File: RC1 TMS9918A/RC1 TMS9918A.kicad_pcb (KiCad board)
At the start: 2 copper layers, 99.1 x 58.4 mm, 21 parts, among them J1 Expansion, J2 ADDRESS, J3 CONFIG, J4 FTDI, U1 R6551, U2 74LS00, U3 74LS138, U4 74LS138, X1 1.8432Mhz, Y1 1.8432Mhz

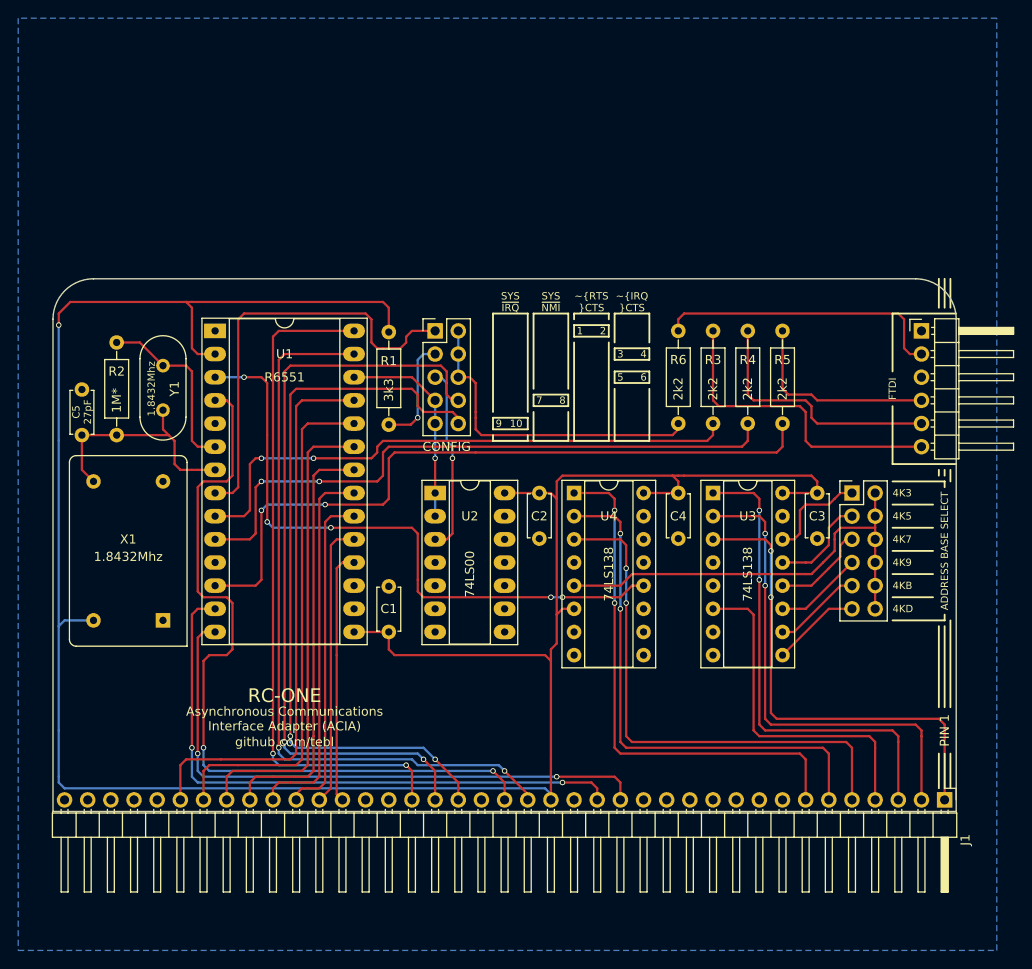
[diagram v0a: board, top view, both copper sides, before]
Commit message: TMS9918 layout
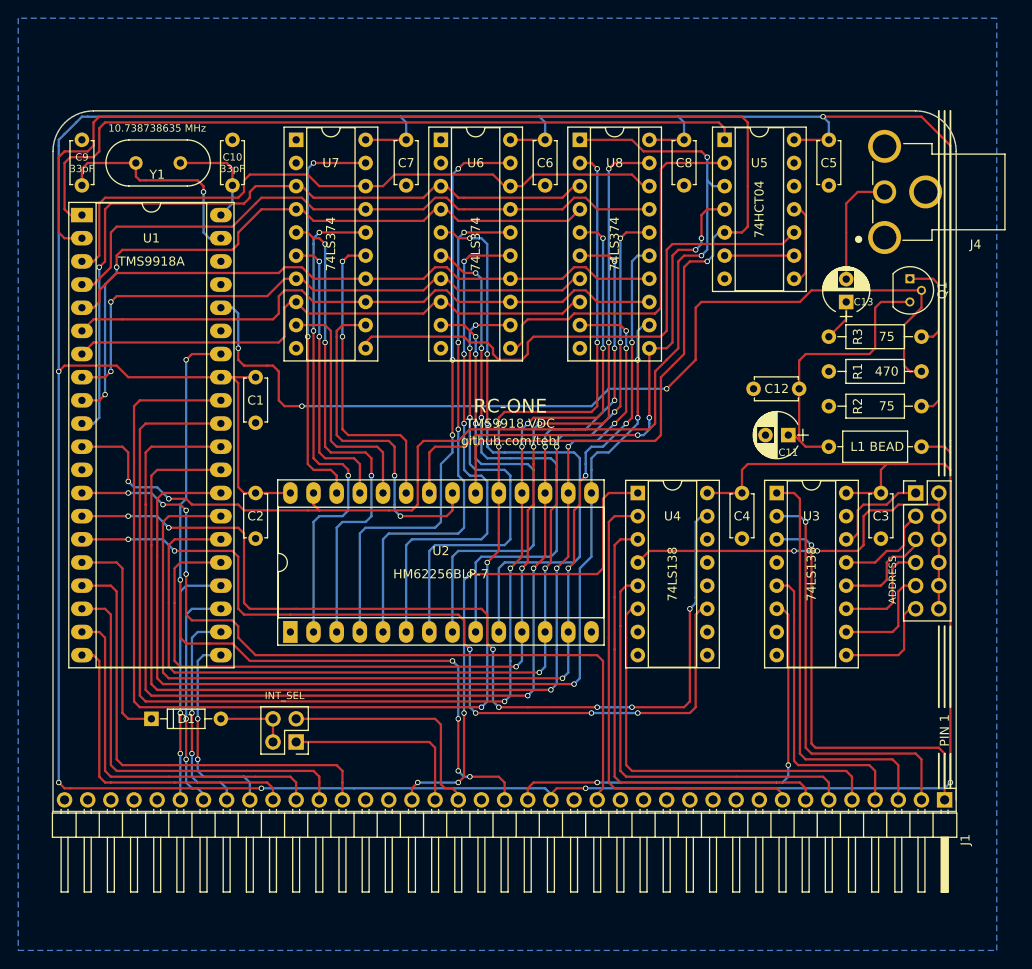
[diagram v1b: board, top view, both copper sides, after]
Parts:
- removed R4, R5, R6: 2k2, Resistors_THT:R_Axial_DIN0207_L6.3mm_D2.5mm_P10.16mm_Horizontal
- removed X1: 1.8432Mhz, Oscillators:Oscillator_DIP-14
- added C10: 33pF, Capacitors_THT:C_Disc_D4.7mm_W2.5mm_P5.00mm, F.Cu at (114.9, 74.9)
- added C11: 22uF, Capacitors_THT:CP_Radial_D5.0mm_P2.50mm, F.Cu at (175.9, 107.3)
- added C12: 100nF, Capacitors_THT:C_Disc_D4.7mm_W2.5mm_P5.00mm, F.Cu at (172.1, 102.2)
- added C13: 220uF, Capacitors_THT:CP_Radial_D5.0mm_P2.50mm, F.Cu at (182.2, 92.7)
- added C6: 100nF, Capacitors_THT:C_Disc_D4.7mm_W2.5mm_P5.00mm, F.Cu at (149.2, 74.9)
- added C7: 100nF, Capacitors_THT:C_Disc_D4.7mm_W2.5mm_P5.00mm, F.Cu at (134.0, 74.9)
- added C8: 100nF, Capacitors_THT:C_Disc_D4.7mm_W2.5mm_P5.00mm, F.Cu at (164.5, 74.9)
- added C9: 33pF, Capacitors_THT:C_Disc_D4.7mm_W2.5mm_P5.00mm, F.Cu at (98.4, 74.9)
- added D1: 1n4148, Diodes_THT:D_DO-35_SOD27_P7.62mm_Horizontal, F.Cu at (106.0, 138.4)
- added L1: BEAD, Inductors_THT:L_Axial_L7.0mm_D3.3mm_P10.16mm_Horizontal_Fastron_MICC, F.Cu at (190.5, 108.6)
- added Q1: 2N3904, TO_SOT_Packages_THT:TO-92_Molded_Narrow, F.Cu at (189.2, 90.2)
- added U5: 74HCT04, Housings_DIP:DIP-14_W7.62mm_Socket, F.Cu at (168.9, 74.9)
- added U6: 74LS374, Housings_DIP:DIP-20_W7.62mm_Socket, F.Cu at (137.8, 74.9)
- added U7: 74LS374, Housings_DIP:DIP-20_W7.62mm_Socket, F.Cu at (121.9, 74.9)
- added U8: 74LS374, Housings_DIP:DIP-20_W7.62mm_Socket, F.Cu at (153.0, 74.9)
- C5: value 27pF -> 100nF
- J3: value CONFIG -> INT_SEL; footprint Pin_Headers:Pin_Header_Straight_2x05_Pitch2.54mm -> Pin_Headers:Pin_Header_Straight_2x02_Pitch2.54mm
- J4: value FTDI -> VIDEO; footprint Pin_Headers:Pin_Header_Angled_1x06_Pitch2.54mm -> RCA:CUI_RCJ-013
- R1: value 3k3 -> 470
- R2: value 1M* -> 75
- R3: value 2k2 -> 75
- U1: value R6551 -> TMS9918A; footprint Housings_DIP:DIP-28_W15.24mm_Socket_LongPads -> Housings_DIP:DIP-40_W15.24mm_Socket_LongPads
- U2: value 74LS00 -> HM62256BLP-7; footprint Housings_DIP:DIP-14_W7.62mm_Socket_LongPads -> Housings_DIP:DIP-28_W15.24mm_Socket_LongPads
- Y1: value 1.8432Mhz -> 10.738738635 MHz
- moved R2 88.5 mm to (190.5, 104.1), turned to 180 degrees
- moved C5 88.1 mm to (180.3, 74.9), turned to 270 degrees
- moved R1 58.6 mm to (190.5, 100.3), turned to 180 degrees
- moved J3 47.6 mm to (121.9, 141.0), turned to 180 degrees
- moved C1 31.5 mm to (117.5, 101.0), turned to 270 degrees
- moved C2 31.1 mm to (117.5, 113.7)
- moved Y1 22.3 mm to (109.2, 77.5), turned to 180 degrees
- moved U2 22.0 mm to (121.3, 128.9), turned to 90 degrees
- moved U1 19.4 mm to (98.4, 83.2)
- moved R3 15.9 mm to (180.3, 96.5), turned to 0 degrees
- moved J4 15.4 mm to (192.4, 80.6), turned to 180 degrees
- moved C3 6.99 mm to (186.1, 113.7)
- moved J2 6.99 mm to (189.9, 113.7)
- moved U3 6.99 mm to (174.6, 113.7)
- moved C4 6.98 mm to (170.8, 113.7)
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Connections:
- net /4K3 renamed /4K2
- net /4K5 renamed /4K4
- net /4K7 renamed /4K6
- net /4K9 renamed /4K8
- net /4KB renamed /4KA
- net /4KD renamed /4KC
- C5 pad 1: Net-(C5-Pad1) -> VCC
- J1 pad 15: /A1 -> (no net)
- J1 pad 8: (no net) -> /A8
- J3 pad 1: Net-(J3-Pad1) -> /~NMI
- J3 pad 2: Net-(J3-Pad2) -> Net-(D1-Pad2)
- J3 pad 3: Net-(J3-Pad3) -> /~IRQ
- J3 pad 4: Net-(J3-Pad2) -> Net-(D1-Pad2)
- J4 pad 1: GND -> Net-(C13-Pad2)
- J4 pad 2: Net-(J4-Pad2) -> GND
- R1 pad 1: VCC -> VIDEO
- R1 pad 2: Net-(J3-Pad3) -> GND
- R2 pad 1: Net-(R2-Pad1) -> Net-(Q1-Pad1)
- R2 pad 2: Net-(C5-Pad1) -> GND
- R3 pad 1: /~CTS -> Net-(C13-Pad1)
- R3 pad 2: Net-(J4-Pad6) -> Net-(Q1-Pad1)
- U1 pad 1: GND -> ~RAS
- U1 pad 10: /TxD -> /VA0
- U1 pad 11: (no net) -> V_R/~W
- U1 pad 12: /RxD -> GND
- U1 pad 14: /A1 -> ~CSW
- U1 pad 15: VCC -> ~CSR
- U1 pad 16: GND -> Net-(D1-Pad1)
- U1 pad 17: GND -> /D0
- U1 pad 18: /D0 -> /D1
- U1 pad 19: /D1 -> /D2
- U1 pad 2: VCC -> ~CAS
- U1 pad 20: /D2 -> /D3
- U1 pad 21: /D3 -> /D4
- U1 pad 22: /D4 -> /D5
- U1 pad 23: /D5 -> /D6
- U1 pad 24: /D6 -> /D7
- U1 pad 25: /D7 -> /VD0
- U1 pad 26: Net-(J3-Pad7) -> /VD1
- U1 pad 27: /PHI2 -> /VD2
- U1 pad 28: /R/~W -> /VD3
- U1 pad 3: ~CS_ACIA -> /VA7
- U1 pad 4: /~RESET -> /VA6
- U1 pad 5: (no net) -> /VA5
- U1 pad 6: Net-(R2-Pad1) -> /VA4
- U1 pad 7: Net-(C5-Pad1) -> /VA3
- U1 pad 8: Net-(J3-Pad1) -> /VA2
- U1 pad 9: /~CTS -> /VA1
- U2 pad 1: Net-(J3-Pad7) -> GND
- U2 pad 10: GND -> /ROW0
- U2 pad 11: (no net) -> /VD0
- U2 pad 12: GND -> /VD1
- U2 pad 13: GND -> /VD2
- U2 pad 14: VCC -> GND
- U2 pad 2: Net-(J3-Pad7) -> /COL5
- U2 pad 3: Net-(J3-Pad5) -> /COL0
- U2 pad 4: GND -> /ROW6
- U2 pad 5: GND -> /ROW5
- U2 pad 6: (no net) -> /ROW4
- U2 pad 7: GND -> /ROW3
- U2 pad 8: (no net) -> /ROW2
- U2 pad 9: GND -> /ROW1
- U3 pad 5: GND -> /A12
- U3 pad 6: /A12 -> /PHI2
- U4 pad 1: /A9 -> /R/~W
- U4 pad 11: (no net) -> ~CSR
- U4 pad 12: ~CS_ACIA -> (no net)
- U4 pad 15: (no net) -> ~CSW
- U4 pad 2: /A10 -> /A8
- U4 pad 3: /A11 -> /A9
- U4 pad 4: GND -> Net-(J2-Pad10)
- U4 pad 5: Net-(J2-Pad10) -> /A10
- U4 pad 6: VCC -> /A11
- Y1 pad 1: Net-(R2-Pad1) -> Net-(C10-Pad2)
- Y1 pad 2: Net-(C5-Pad1) -> Net-(C9-Pad2)
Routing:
- net VCC: track 267.2 -> 448.2 mm, vias 1 -> 6
- net ~CAS: track 0.00 -> 157.0 mm, vias 0 -> 1
- net /VD7: track 0.00 -> 152.6 mm, vias 0 -> 6
- net /VD6: track 0.00 -> 140.8 mm, vias 0 -> 6
- net /VD5: track 0.00 -> 134.6 mm, vias 0 -> 6
- net V_R/~W: track 0.00 -> 127.7 mm, vias 0 -> 4
- net /VD4: track 0.00 -> 124.4 mm, vias 0 -> 6
- net /VD0: track 0.00 -> 120.8 mm, vias 0 -> 6
- net /VD2: track 0.00 -> 119.0 mm, vias 0 -> 5
- net /VD3: track 0.00 -> 116.8 mm, vias 0 -> 3
- net /VD1: track 0.00 -> 116.8 mm, vias 0 -> 6
- net ~CSW: track 0.00 -> 106.8 mm, vias 0 -> 7
- net VIDEO: track 0.00 -> 106.0 mm, vias 0 -> 3
- net ~CSR: track 0.00 -> 95.7 mm, vias 0 -> 6
- net ~RAS: track 0.00 -> 84.5 mm
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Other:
- board size 99.1 x 58.4 mm -> 99.1 x 76.8 mm
- board text added: "$2800"
- board text added: "$4800"
- board text added: "$6800"
- board text added: "$8800"
- board text added: "$A800"
- board text added: "$C800"
- board text added: "1-2 NMI"
- board text added: "3-4 IRQ"
- board text added: "4K2"
- board text added: "4K4"
- board text added: "4K6"
- board text added: "4K8"
- board text added: "4KA"
- board text added: "4KC"
- board text added: "ADDRESS"
- board text added: "COL LATCH"
- board text added: "DATA LATCH"
- board text added: "HEX INVERTER"
- board text added: "INTERRUPT"
- board text added: "ROW LATCH"
- board text added: "STATIC RAM"
- board text added: "TMS9918"
- board text added: "TMS9918 VDC"
- board text added: "VIDEO DISPLAY CONTROLLER (VDC)"
- board text removed: "$1C $1D $1E $1F"
- board text removed: "$3600"
- board text removed: "$5600"
- board text removed: "$7600"
- board text removed: "$9600"
- board text removed: "$B600"
- board text removed: "$D600"
- board text removed: "$x600 $x601 $x602 $x603"
- board text removed: "0"
- board text removed: "1"
- board text removed: "10"
- board text removed: "2"
- board text removed: "3"
- board text removed: "4"
- board text removed: "4800 7200 9600 19200"
- board text removed: "4K3"
- board text removed: "4K5"
- board text removed: "4K7"
- board text removed: "4K9"
- board text removed: "4KB"
- board text removed: "4KD"
- board text removed: "5"
- board text removed: "6"
- board text removed: "6551 ACIA"
- board text removed: "7"
- board text removed: "8"
- board text removed: "8-N-1"
- board text removed: "9"
- board text removed: "ADDRESS BASE SELECT"
- board text removed: "Asynchronous Communications Interface Adapter (ACIA)"
- board text removed: "COMMAND"
- board text removed: "CONFIGURATION"
- board text removed: "CONTROL"
- board text removed: "CRYSTAL"
- board text removed: "DATA STATUS COMMAND CONTROL"
- board text removed: "DTR"
- board text removed: "FE"
- board text removed: "FTDI"
- board text removed: "GND"
- board text removed: "IRD"
- board text removed: "IRQ"
- board text removed: "NAND GATES"
- board text removed: "OVRN"
- board text removed: "PE"
- board text removed: "PMC"
- board text removed: "PMC0"
- board text removed: "PMC1"
- board text removed: "PME"
- board text removed: "RCS"
- board text removed: "RDRF"
- board text removed: "REGISTERS"
- board text removed: "REM"
- board text removed: "Revision B"
- board text removed: "RxD"
- board text removed: "SBN"
- board text removed: "SBR"
- board text removed: "SBR0"
- board text removed: "SBR1"
- board text removed: "SBR2"
- board text removed: "SBR3"
- board text removed: "STATUS"
- board text removed: "SYS ~IRQ"
- board text removed: "SYS ~NMI"
- board text removed: "TDRE"
- board text removed: "TIC"
- board text removed: "TIC0"
- board text removed: "TIC1"
- board text removed: "TTL OSCILLATOR"
- board text removed: "TxD"
- board text removed: "WL"
- board text removed: "WL0"
- board text removed: "WL1"
- board text removed: "~CTS"
- board text removed: "~DCD"
- board text removed: "~DSR"
- board text removed: "~IRQ ~CTS"
- board text removed: "~RTS"
- board text removed: "~RTS ~CTS"
